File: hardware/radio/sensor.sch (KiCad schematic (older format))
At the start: 5 parts, among them U501 SN74AUP1T32, U502 ADXL375

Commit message: Assign testpoint footprints
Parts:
- C501, C502: footprint (none) -> Capacitors_SMD:C_0603
- FB501: footprint (none) -> Resistors_SMD:R_0603
- U501: footprint (none) -> Housings_SOT-23_SOT-143_TSOT-6:SOT-23-5
- U502: footprint (none) -> footprints_:LGA-14_(CC-14-1)
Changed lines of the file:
@@
 F 0 "U502" H 5750 3950 60  0000 C CNN
 F 1 "ADXL375" H 5750 3850 60  0000 C CNN
-F 2 "" H 5750 2750 60  0000 C CNN
+F 2 "footprints_:LGA-14_(CC-14-1)" H 5750 2750 60  0001 C CNN
 F 3 "" H 5750 2750 60  0000 C CNN
 	1    5750 3550
@@
 Connection ~ 4700 3750
 $Comp
-L GND #PWR043
+L GND #PWR044
 U 1 1 55EC1E55
 P 4700 4150
-F 0 "#PWR043" H 4700 3900 50  0001 C CNN
+F 0 "#PWR044" H 4700 3900 50  0001 C CNN
 F 1 "GND" H 4700 4000 50  0000 C CNN
 F 2 "" H 4700 4150 60  0000 C CNN
@@
 $EndComp
 $Comp
-L VCC #PWR044
+L VCC #PWR045
 U 1 1 55EC1E6B
 P 3250 2950
-F 0 "#PWR044" H 3250 2800 50  0001 C CNN
+F 0 "#PWR045" H 3250 2800 50  0001 C CNN
 F 1 "VCC" H 3250 3100 50  0000 C CNN
 F 2 "" H 3250 2950 60  0000 C CNN
@@
 F 0 "U501" H 8450 3500 60  0000 C CNN
 F 1 "SN74AUP1T32" H 8650 3200 60  0000 C CNN
-F 2 "" H 8450 3450 60  0000 C CNN
+F 2 "Housings_SOT-23_SOT-143_TSOT-6:SOT-23-5" H 8450 3450 60  0001 C CNN
 F 3 "" H 8450 3450 60  0000 C CNN
 	1    8450 3450
@@
 	9050 3850 9050 3800
 $Comp
-L VCC #PWR045
+L VCC #PWR046
 U 1 1 55EC3D01
 P 9050 3800
-F 0 "#PWR045" H 9050 3650 50  0001 C CNN
+F 0 "#PWR046" H 9050 3650 50  0001 C CNN
 F 1 "VCC" H 9050 3950 50  0000 C CNN
 F 2 "" H 9050 3800 60  0000 C CNN
@@
 $EndComp
 $Comp
-L GND #PWR046
+L GND #PWR047
 U 1 1 55EC3D19
 P 9150 3850
-F 0 "#PWR046" H 9150 3600 50  0001 C CNN
+F 0 "#PWR047" H 9150 3600 50  0001 C CNN
 F 1 "GND" H 9150 3700 50  0000 C CNN
 F 2 "" H 9150 3850 60  0000 C CNN
@@
 F 0 "FB501" H 3900 3400 50  0000 C CNN
 F 1 "FILTER" H 3900 3150 50  0000 C CNN
-F 2 "" H 3900 3250 60  0000 C CNN
+F 2 "Resistors_SMD:R_0603" H 3900 3250 60  0001 C CNN
 F 3 "" H 3900 3250 60  0000 C CNN
 	1    3900 3250
@@
 F 0 "C501" H 3275 3950 50  0000 L CNN
 F 1 "100n" H 3275 3750 50  0000 L CNN
-F 2 "" H 3288 3700 30  0000 C CNN
+F 2 "Capacitors_SMD:C_0603" H 3288 3700 30  0001 C CNN
 F 3 "" H 3250 3850 60  0000 C CNN
 	1    3250 3850
@@
 F 0 "C502" H 4425 3950 50  0000 L CNN
 F 1 "100n" H 4425 3750 50  0000 L CNN
-F 2 "" H 4438 3700 30  0000 C CNN
+F 2 "Capacitors_SMD:C_0603" H 4438 3700 30  0001 C CNN
 F 3 "" H 4400 3850 60  0000 C CNN
 	1    4400 3850
@@
 	3250 4000 3250 4150
 $Comp
-L GND #PWR047
+L GND #PWR048
 U 1 1 55EC414E
 P 3250 4150
-F 0 "#PWR047" H 3250 3900 50  0001 C CNN
+F 0 "#PWR048" H 3250 3900 50  0001 C CNN
 F 1 "GND" H 3250 4000 50  0000 C CNN
 F 2 "" H 3250 4150 60  0000 C CNN
@@
 $EndComp
 $Comp
-L GND #PWR048
+L GND #PWR049
 U 1 1 55EC416C
 P 4400 4150
-F 0 "#PWR048" H 4400 3900 50  0001 C CNN
+F 0 "#PWR049" H 4400 3900 50  0001 C CNN
 F 1 "GND" H 4400 4000 50  0000 C CNN
 F 2 "" H 4400 4150 60  0000 C CNN

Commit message: Work on laying out TPs
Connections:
- net VCC: no longer C501.1, FB501.1, U502.1 (VDDIO)
- new net VCC_ACC: C501.1, FB501.1, U502.1 (VDDIO)
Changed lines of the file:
@@
 	3250 3350 4850 3350
 Wire Wire Line
-	4250 3250 4850 3250
+	4250 3250 4400 3250
+Wire Wire Line
+	4400 3250 4850 3250
 Wire Wire Line
 	4850 3550 4700 3550
 Wire Wire Line
-	4700 3550 4700 4150
+	4700 3550 4700 3650
+Wire Wire Line
+	4700 3650 4700 3750
+Wire Wire Line
+	4700 3750 4700 4150
 Wire Wire Line
 	4850 3650 4700 3650
@@
 Connection ~ 4700 3750
 $Comp
-L GND #PWR044
+L GND #PWR039
 U 1 1 55EC1E55
 P 4700 4150
-F 0 "#PWR044" H 4700 3900 50  0001 C CNN
+F 0 "#PWR039" H 4700 3900 50  0001 C CNN
 F 1 "GND" H 4700 4000 50  0000 C CNN
 F 2 "" H 4700 4150 60  0000 C CNN
 F 3 "" H 4700 4150 60  0000 C CNN
 	1    4700 4150
-	1    0    0    -1
-$EndComp
-$Comp
-L VCC #PWR045
-U 1 1 55EC1E6B
-P 3250 2950
-F 0 "#PWR045" H 3250 2800 50  0001 C CNN
-F 1 "VCC" H 3250 3100 50  0000 C CNN
-F 2 "" H 3250 2950 60  0000 C CNN
-F 3 "" H 3250 2950 60  0000 C CNN
-	1    3250 2950
 	1    0    0    -1
 $EndComp
@@
 $EndComp
 Wire Wire Line
-	7400 3050 9700 3050
+	7400 3050 9300 3050
+Wire Wire Line
+	9300 3050 9700 3050
 Wire Wire Line
 	8600 3100 9150 3100
@@
 	9050 3850 9050 3800
 $Comp
-L VCC #PWR046
+L VCC #PWR041
 U 1 1 55EC3D01
 P 9050 3800
-F 0 "#PWR046" H 9050 3650 50  0001 C CNN
+F 0 "#PWR041" H 9050 3650 50  0001 C CNN
 F 1 "VCC" H 9050 3950 50  0000 C CNN
 F 2 "" H 9050 3800 60  0000 C CNN
@@
 $EndComp
 $Comp
-L GND #PWR047
+L GND #PWR042
 U 1 1 55EC3D19
 P 9150 3850
-F 0 "#PWR047" H 9150 3600 50  0001 C CNN
+F 0 "#PWR042" H 9150 3600 50  0001 C CNN
 F 1 "GND" H 9150 3700 50  0000 C CNN
 F 2 "" H 9150 3850 60  0000 C CNN
@@
 Connection ~ 4400 3250
 Wire Wire Line
-	3250 2950 3250 3700
+	3250 3100 3250 3250
+Wire Wire Line
+	3250 3250 3250 3350
+Wire Wire Line
+	3250 3350 3250 3700
 Wire Wire Line
 	3550 3250 3250 3250
@@
 	4400 4000 4400 4150
 Wire Wire Line
-	3250 4000 3250 4150
+	3250 4000 3250 4100
+Wire Wire Line
+	3250 4100 3250 4150
 $Comp
-L GND #PWR048
+L GND #PWR043
 U 1 1 55EC414E
 P 3250 4150
-F 0 "#PWR048" H 3250 3900 50  0001 C CNN
+F 0 "#PWR043" H 3250 3900 50  0001 C CNN
 F 1 "GND" H 3250 4000 50  0000 C CNN
 F 2 "" H 3250 4150 60  0000 C CNN
@@
 $EndComp
 $Comp
-L GND #PWR049
+L GND #PWR044
 U 1 1 55EC416C
 P 4400 4150
-F 0 "#PWR049" H 4400 3900 50  0001 C CNN
+F 0 "#PWR044" H 4400 3900 50  0001 C CNN
 F 1 "GND" H 4400 4000 50  0000 C CNN
 F 2 "" H 4400 4150 60  0000 C CNN
@@
 $EndComp
 Text HLabel 2850 3100 0    60   Input ~ 0
-VCC
+VCC_ACC
 Wire Wire Line
 	2850 3100 3250 3100
-Connection ~ 3250 3100
 Wire Wire Line
 	3250 4100 2900 4100

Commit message: Give sensor own power net
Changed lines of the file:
@@
 	3250 3350 4850 3350
 Wire Wire Line
-	4250 3250 4400 3250
-Wire Wire Line
-	4400 3250 4850 3250
+	4250 3250 4850 3250
 Wire Wire Line
 	4850 3550 4700 3550
 Wire Wire Line
-	4700 3550 4700 3650
-Wire Wire Line
-	4700 3650 4700 3750
-Wire Wire Line
-	4700 3750 4700 4150
+	4700 3550 4700 4150
 Wire Wire Line
 	4850 3650 4700 3650
@@
 $EndComp
 Wire Wire Line
-	7400 3050 9300 3050
-Wire Wire Line
-	9300 3050 9700 3050
+	7400 3050 9700 3050
 Wire Wire Line
 	8600 3100 9150 3100
@@
 	9050 3850 9050 3800
 $Comp
-L VCC #PWR041
+L VCC #PWR040
 U 1 1 55EC3D01
 P 9050 3800
-F 0 "#PWR041" H 9050 3650 50  0001 C CNN
+F 0 "#PWR040" H 9050 3650 50  0001 C CNN
 F 1 "VCC" H 9050 3950 50  0000 C CNN
 F 2 "" H 9050 3800 60  0000 C CNN
@@
 $EndComp
 $Comp
-L GND #PWR042
+L GND #PWR041
 U 1 1 55EC3D19
 P 9150 3850
-F 0 "#PWR042" H 9150 3600 50  0001 C CNN
+F 0 "#PWR041" H 9150 3600 50  0001 C CNN
 F 1 "GND" H 9150 3700 50  0000 C CNN
 F 2 "" H 9150 3850 60  0000 C CNN
@@
 Connection ~ 4400 3250
 Wire Wire Line
-	3250 3100 3250 3250
-Wire Wire Line
-	3250 3250 3250 3350
-Wire Wire Line
-	3250 3350 3250 3700
+	3250 3100 3250 3700
 Wire Wire Line
 	3550 3250 3250 3250
@@
 	4400 4000 4400 4150
 Wire Wire Line
-	3250 4000 3250 4100
-Wire Wire Line
-	3250 4100 3250 4150
+	3250 4000 3250 4150
 $Comp
-L GND #PWR043
+L GND #PWR042
 U 1 1 55EC414E
 P 3250 4150
-F 0 "#PWR043" H 3250 3900 50  0001 C CNN
+F 0 "#PWR042" H 3250 3900 50  0001 C CNN
 F 1 "GND" H 3250 4000 50  0000 C CNN
 F 2 "" H 3250 4150 60  0000 C CNN
@@
 $EndComp
 $Comp
-L GND #PWR044
+L GND #PWR043
 U 1 1 55EC416C
 P 4400 4150
-F 0 "#PWR044" H 4400 3900 50  0001 C CNN
+F 0 "#PWR043" H 4400 3900 50  0001 C CNN
 F 1 "GND" H 4400 4000 50  0000 C CNN
 F 2 "" H 4400 4150 60  0000 C CNN

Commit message: Routing finalized
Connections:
- net VCC is gone; now on net VCC_ACC: U501.5 (VCC)
- net SCLK renamed SCL
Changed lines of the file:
@@
 Connection ~ 4700 3750
 $Comp
-L GND #PWR037
+L GND #PWR036
 U 1 1 55EC1E55
 P 4700 4150
-F 0 "#PWR037" H 4700 3900 50  0001 C CNN
+F 0 "#PWR036" H 4700 3900 50  0001 C CNN
 F 1 "GND" H 4700 4000 50  0000 C CNN
 F 2 "" H 4700 4150 60  0000 C CNN
@@
 	9050 3850 9050 3800
 $Comp
-L VCC #PWR038
-U 1 1 55EC3D01
-P 9050 3800
-F 0 "#PWR038" H 9050 3650 50  0001 C CNN
-F 1 "VCC" H 9050 3950 50  0000 C CNN
-F 2 "" H 9050 3800 60  0000 C CNN
-F 3 "" H 9050 3800 60  0000 C CNN
-	1    9050 3800
-	1    0    0    -1
-$EndComp
-$Comp
-L GND #PWR039
+L GND #PWR037
 U 1 1 55EC3D19
 P 9150 3850
-F 0 "#PWR039" H 9150 3600 50  0001 C CNN
+F 0 "#PWR037" H 9150 3600 50  0001 C CNN
 F 1 "GND" H 9150 3700 50  0000 C CNN
 F 2 "" H 9150 3850 60  0000 C CNN
@@
 	6650 3550 7400 3550
 Text HLabel 7400 3550 2    60   Input ~ 0
-SCLK
+SCL
 Wire Wire Line
 	6650 3750 7400 3750
@@
 	3250 4000 3250 4150
 $Comp
-L GND #PWR040
+L GND #PWR038
 U 1 1 55EC414E
 P 3250 4150
-F 0 "#PWR040" H 3250 3900 50  0001 C CNN
+F 0 "#PWR038" H 3250 3900 50  0001 C CNN
 F 1 "GND" H 3250 4000 50  0000 C CNN
 F 2 "" H 3250 4150 60  0000 C CNN
@@
 $EndComp
 $Comp
-L GND #PWR041
+L GND #PWR039
 U 1 1 55EC416C
 P 4400 4150
-F 0 "#PWR041" H 4400 3900 50  0001 C CNN
+F 0 "#PWR039" H 4400 3900 50  0001 C CNN
 F 1 "GND" H 4400 4000 50  0000 C CNN
 F 2 "" H 4400 4150 60  0000 C CNN
@@
 Text HLabel 2900 4100 0    60   Input ~ 0
 GND
+Text Label 3250 3100 0    60   ~ 0
+VCC_ACC
+Text Label 8650 3850 0    60   ~ 0
+VCC_ACC
 $EndSCHEMATC

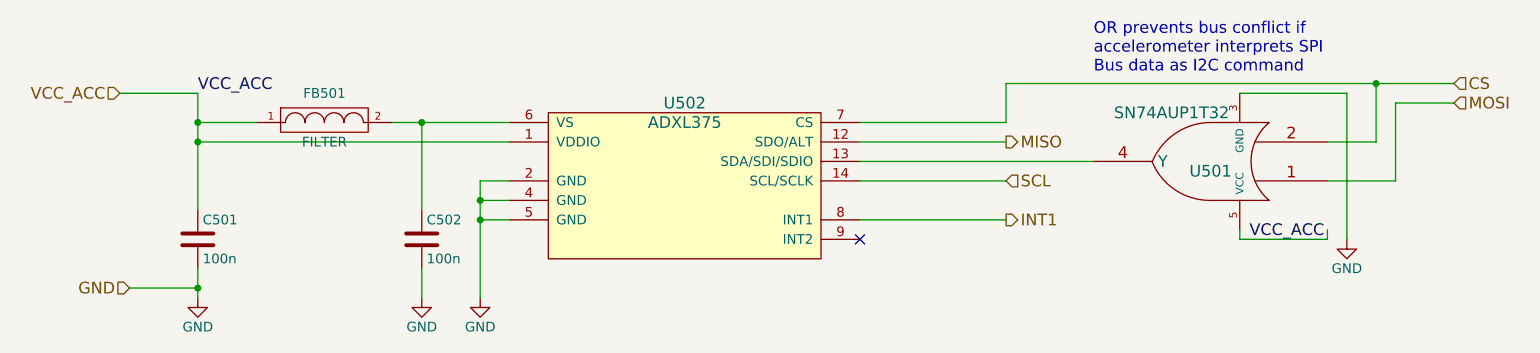
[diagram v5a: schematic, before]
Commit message: Compress schematics for printouts
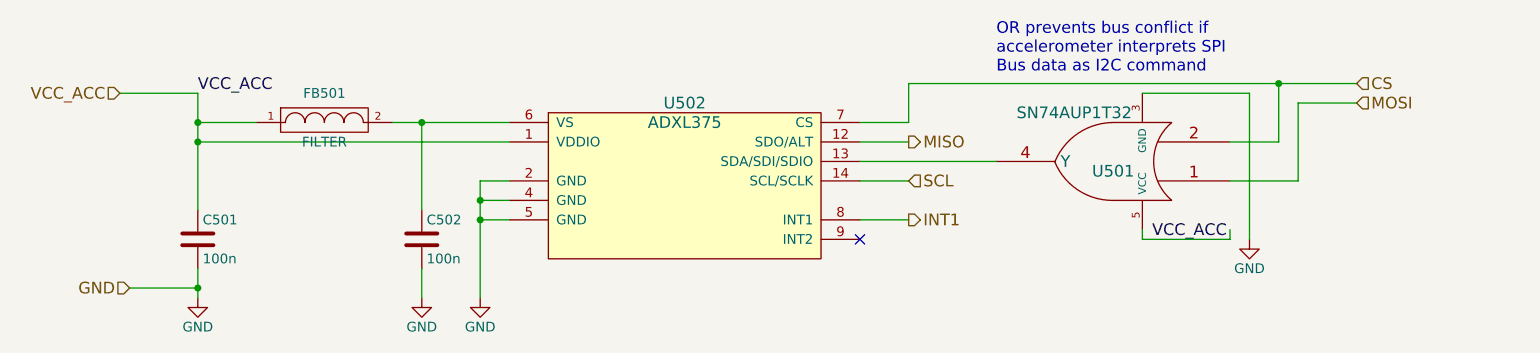
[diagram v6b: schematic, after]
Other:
- moved on the sheet: U501
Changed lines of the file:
@@
 	3250 3350 4850 3350
 Wire Wire Line
-	4250 3250 4850 3250
+	4250 3250 4400 3250
+Wire Wire Line
+	4400 3250 4850 3250
 Wire Wire Line
 	4850 3550 4700 3550
 Wire Wire Line
-	4700 3550 4700 4150
+	4700 3550 4700 3650
+Wire Wire Line
+	4700 3650 4700 3750
+Wire Wire Line
+	4700 3750 4700 4150
 Wire Wire Line
 	4850 3650 4700 3650
@@
 $EndComp
 Wire Wire Line
-	6650 3450 7850 3450
+	6650 3450 7350 3450
 Wire Wire Line
-	7400 3250 6650 3250
+	6900 3250 6650 3250
 Wire Wire Line
-	7400 3050 7400 3250
+	6900 3050 6900 3250
 Wire Wire Line
-	9300 3050 9300 3350
+	8800 3050 8800 3350
 Wire Wire Line
-	9300 3350 9050 3350
+	8800 3350 8550 3350
 Wire Wire Line
-	9050 3550 9400 3550
+	8550 3550 8900 3550
 $Comp
 L SN74AUP1T32 U501
 U 1 1 55EC3854
-P 8450 3450
-F 0 "U501" H 8450 3500 60  0000 C CNN
-F 1 "SN74AUP1T32" H 8650 3200 60  0000 C CNN
-F 2 "Housings_SOT-23_SOT-143_TSOT-6:SOT-23-5" H 8450 3450 60  0001 C CNN
-F 3 "" H 8450 3450 60  0000 C CNN
-	1    8450 3450
+P 7950 3450
+F 0 "U501" H 7950 3500 60  0000 C CNN
+F 1 "SN74AUP1T32" H 8150 3200 60  0000 C CNN
+F 2 "Housings_SOT-23_SOT-143_TSOT-6:SOT-23-5" H 7950 3450 60  0001 C CNN
+F 3 "" H 7950 3450 60  0000 C CNN
+	1    7950 3450
 	-1   0    0    1
 $EndComp
 Wire Wire Line
-	7400 3050 9700 3050
+	6900 3050 8800 3050
 Wire Wire Line
-	8600 3100 9150 3100
+	8800 3050 9200 3050
 Wire Wire Line
-	9150 3100 9150 3850
+	8100 3100 8650 3100
 Wire Wire Line
-	8600 3800 8600 3850
+	8650 3100 8650 3850
 Wire Wire Line
-	8600 3850 9050 3850
+	8100 3800 8100 3850
 Wire Wire Line
-	9050 3850 9050 3800
+	8100 3850 8550 3850
+Wire Wire Line
+	8550 3850 8550 3800
 $Comp
 L GND #PWR037
 U 1 1 55EC3D19
-P 9150 3850
-F 0 "#PWR037" H 9150 3600 50  0001 C CNN
-F 1 "GND" H 9150 3700 50  0000 C CNN
-F 2 "" H 9150 3850 60  0000 C CNN
-F 3 "" H 9150 3850 60  0000 C CNN
-	1    9150 3850
+P 8650 3850
+F 0 "#PWR037" H 8650 3600 50  0001 C CNN
+F 1 "GND" H 8650 3700 50  0000 C CNN
+F 2 "" H 8650 3850 60  0000 C CNN
+F 3 "" H 8650 3850 60  0000 C CNN
+	1    8650 3850
 	1    0    0    -1
 $EndComp
-Connection ~ 9300 3050
+Connection ~ 8800 3050
 Wire Wire Line
-	9400 3550 9400 3150
+	8900 3550 8900 3150
 Wire Wire Line
-	9400 3150 9700 3150
-Text Notes 7850 3000 0    60   ~ 0
+	8900 3150 9200 3150
+Text Notes 7350 3000 0    60   ~ 0
 OR prevents bus conflict if \naccelerometer interprets SPI\nBus data as I2C command
-Text HLabel 9700 3050 2    60   Input ~ 0
+Text HLabel 9200 3050 2    60   Input ~ 0
 CS
-Text HLabel 9700 3150 2    60   Input ~ 0
+Text HLabel 9200 3150 2    60   Input ~ 0
 MOSI
 Wire Wire Line
-	6650 3350 7400 3350
-Text HLabel 7400 3350 2    60   Output ~ 0
+	6650 3350 6900 3350
+Text HLabel 6900 3350 2    60   Output ~ 0
 MISO
 Wire Wire Line
-	6650 3550 7400 3550
-Text HLabel 7400 3550 2    60   Input ~ 0
+	6650 3550 6900 3550
+Text HLabel 6900 3550 2    60   Input ~ 0
 SCL
 Wire Wire Line
-	6650 3750 7400 3750
-Text HLabel 7400 3750 2    60   Output ~ 0
+	6650 3750 6900 3750
+Text HLabel 6900 3750 2    60   Output ~ 0
 INT1
 NoConn ~ 6650 3850
@@
 Connection ~ 4400 3250
 Wire Wire Line
-	3250 3100 3250 3700
+	3250 3100 3250 3250
+Wire Wire Line
+	3250 3250 3250 3350
+Wire Wire Line
+	3250 3350 3250 3700
 Wire Wire Line
 	3550 3250 3250 3250
@@
 	4400 4000 4400 4150
 Wire Wire Line
-	3250 4000 3250 4150
+	3250 4000 3250 4100
+Wire Wire Line
+	3250 4100 3250 4150
 $Comp
 L GND #PWR038
@@
 Text Label 3250 3100 0    60   ~ 0
 VCC_ACC
-Text Label 8650 3850 0    60   ~ 0
+Text Label 8150 3850 0    60   ~ 0
 VCC_ACC
 $EndSCHEMATC

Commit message: Compress schematics for screenshots
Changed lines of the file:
@@
 	3250 3350 4850 3350
 Wire Wire Line
-	4250 3250 4400 3250
-Wire Wire Line
-	4400 3250 4850 3250
+	4250 3250 4850 3250
 Wire Wire Line
 	4850 3550 4700 3550
 Wire Wire Line
-	4700 3550 4700 3650
-Wire Wire Line
-	4700 3650 4700 3750
-Wire Wire Line
-	4700 3750 4700 4150
+	4700 3550 4700 4150
 Wire Wire Line
 	4850 3650 4700 3650
@@
 $EndComp
 Wire Wire Line
-	6900 3050 8800 3050
-Wire Wire Line
-	8800 3050 9200 3050
+	6900 3050 9200 3050
 Wire Wire Line
 	8100 3100 8650 3100
@@
 Connection ~ 4400 3250
 Wire Wire Line
-	3250 3100 3250 3250
-Wire Wire Line
-	3250 3250 3250 3350
-Wire Wire Line
-	3250 3350 3250 3700
+	3250 3100 3250 3700
 Wire Wire Line
 	3550 3250 3250 3250
@@
 	4400 4000 4400 4150
 Wire Wire Line
-	3250 4000 3250 4100
-Wire Wire Line
-	3250 4100 3250 4150
+	3250 4000 3250 4150
 $Comp
 L GND #PWR038
